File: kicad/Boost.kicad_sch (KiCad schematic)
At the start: 14 parts, among them U15 6.8uH, U16 SX1308

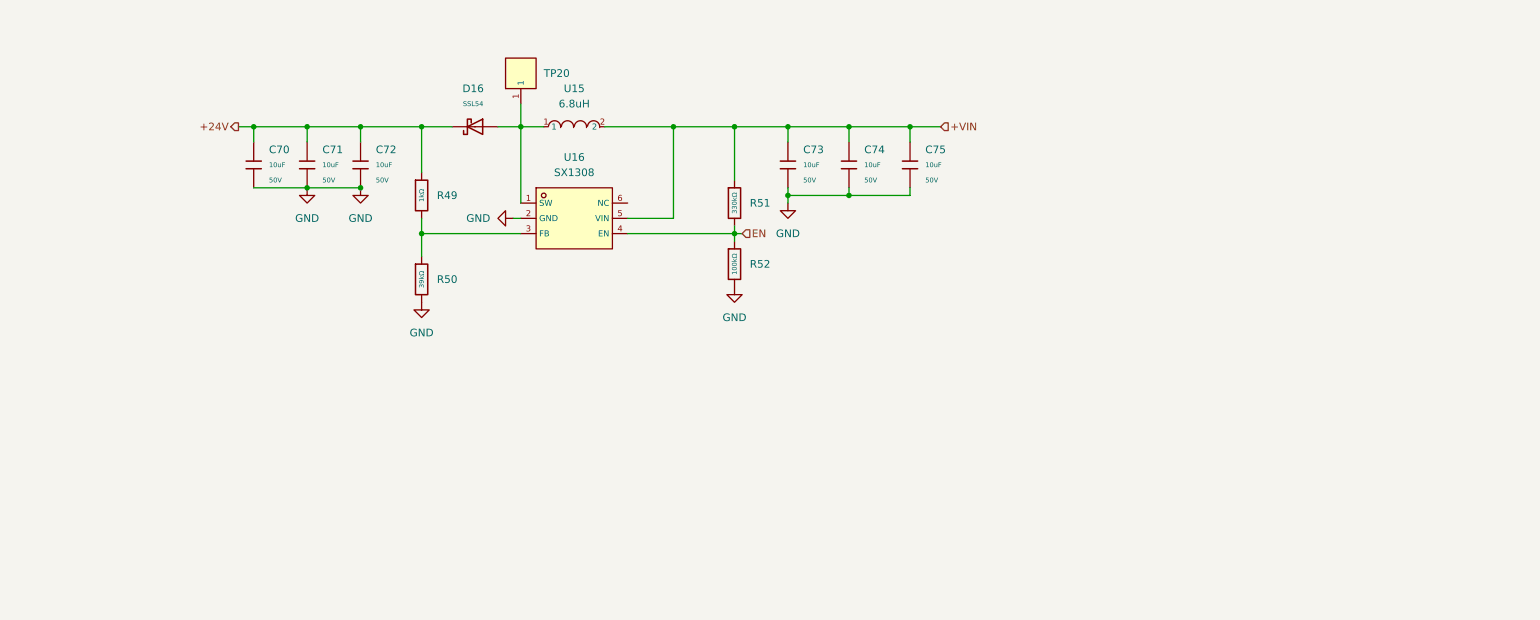
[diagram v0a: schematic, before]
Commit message: Footprint routing completed
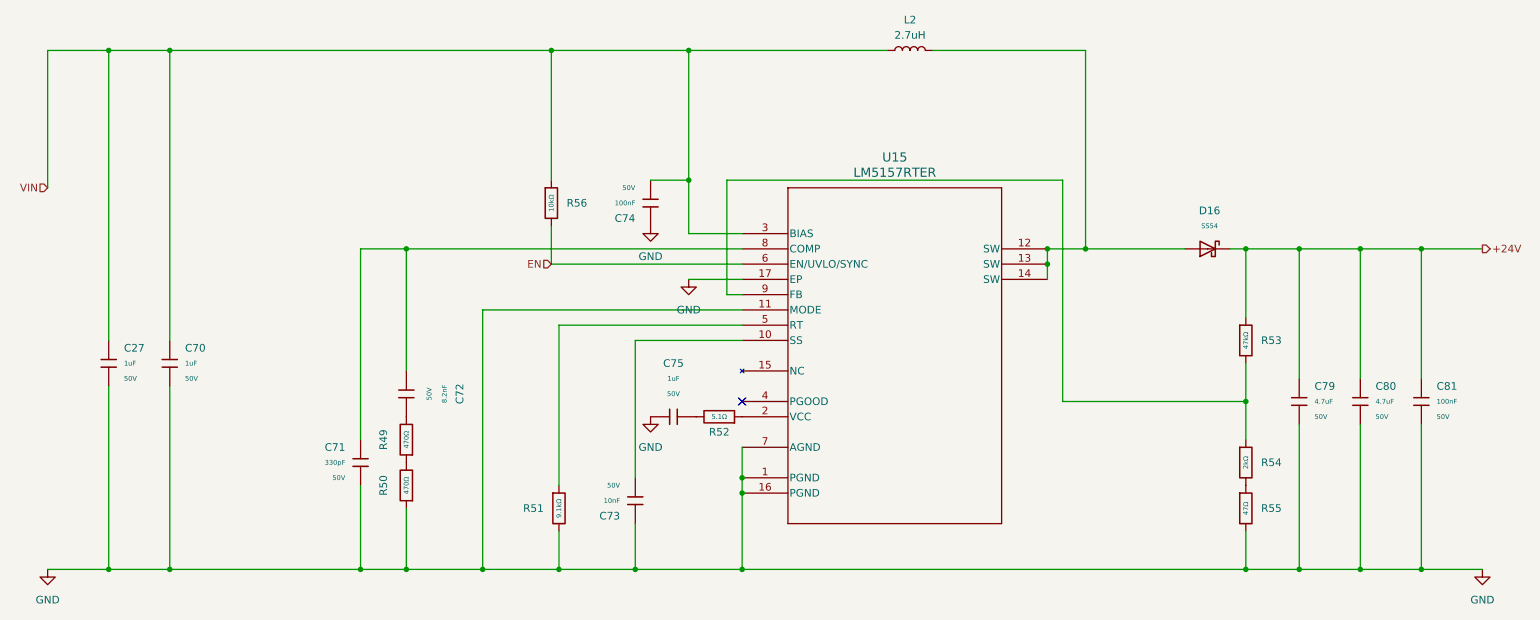
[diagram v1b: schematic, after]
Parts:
- removed C70, C71, C72, C73, C74, C75: 10uF, PCM_JLCPCB:C_0805, symbol 4in-power:0805,10uF,(2)
- removed D16: SSL54, PCM_JLCPCB:D_SMA, symbol 4in-power:Schottky,SSL54
- removed R49: 1kΩ, PCM_JLCPCB:R_0402, symbol 4in-power:0402,1kΩ
- removed R50: 39kΩ, PCM_JLCPCB:R_0402, symbol 4in-power:0402,39kΩ
- removed R51: 330kΩ, PCM_JLCPCB:R_0805, symbol 4in-power:0805,330kΩ
- removed R52: 100kΩ, PCM_JLCPCB:R_0805, symbol 4in-power:0805,100kΩ
- removed TP20: RH-5015, 4in-power:SMD_RH-5015, symbol 4in-power:RH-5015
- removed U15: 6.8uH, 4in-power:IND-SMD_L5.4-W5.2_SLO0530H6R8MTT, symbol 4in-power:SLO0530H6R8MTT
- removed U16: SX1308, 4in-power:SOT-23-6_L2.9-W1.6-P0.95-LS2.8-BL, symbol 4in-power:SX1308
- added C27, C70: 1uF, PCM_JLCPCB:C_0805, symbol PCM_JLCPCB-Capacitors:0805,1uF
- added C71: 330pF, PCM_JLCPCB:C_0603, symbol PCM_JLCPCB-Capacitors:0603,330pF
- added C72: 8.2nF, PCM_JLCPCB:C_0603, symbol PCM_JLCPCB-Capacitors:0603,8.2nF
- added C73: 10nF, PCM_JLCPCB:C_0402, symbol PCM_JLCPCB-Capacitors:0402,10nF
- added C74, C81: 100nF, PCM_JLCPCB:C_0402, symbol PCM_JLCPCB-Capacitors:0402,100nF,(2)
- added C75: 1uF, PCM_JLCPCB:C_0603, symbol PCM_JLCPCB-Capacitors:0603,1uF
- added C79, C80: 4.7uF, PCM_JLCPCB:C_1206, symbol PCM_JLCPCB-Capacitors:1206,4.7uF
- added D16: SS54, PCM_JLCPCB:D_SMA, symbol PCM_JLCPCB-Diodes:Schottky,SS54
- added L2: 2.7uH, 4in-power:IND-SMD_L7.5-W7.5_XAL7030, symbol Device:L
- added R49, R50: 470Ω, PCM_JLCPCB:R_0603, symbol PCM_JLCPCB-Resistors:0603,470Ω
- added R51: 9.1kΩ, PCM_JLCPCB:R_0603, symbol PCM_JLCPCB-Resistors:0603,9.1kΩ
- added R52: 5.1Ω, PCM_JLCPCB:R_0603, symbol PCM_JLCPCB-Resistors:0603,5.1Ω
- added R53: 47kΩ, PCM_JLCPCB:R_0402, symbol PCM_JLCPCB-Resistors:0402,47kΩ
- added R54: 2kΩ, PCM_JLCPCB:R_0402, symbol PCM_JLCPCB-Resistors:0402,2kΩ
- added R55: 47Ω, PCM_JLCPCB:R_0402, symbol PCM_JLCPCB-Resistors:0402,47Ω
- added R56: 10kΩ, PCM_JLCPCB:R_0402, symbol 4in-power:0402,10kΩ
- added U15: LM5157RTER, 4in-power:WQFN-16_L3.0-W3.0-P0.50-TL-EP1.7, symbol Customer:LM5157RTER
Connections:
- net +24V: now also C79.1, C80.1, C81.1, D16.1, R53.1
- net EN: now also R56.2, U15.6 (EN/UVLO/SYNC)
- net GND: now also C27.2, C70.2, C71.1, C73.1, C74.2, C75.2, C79.2, C80.2, C81.2, R50.1, R51.2, R55.2, U15.1 (PGND), U15.11 (MODE), U15.16 (PGND), U15.17 (EP), U15.7 (AGND)
- new net: R51.1, U15.5 (RT)
- new net: C71.2, C72.1, U15.8 (COMP)
- new net: C72.2, R49.2
- new net: R53.2, R54.1, U15.9 (FB)
- new net: R54.2, R55.1
- new net: D16.2, L2.2, U15.12 (SW), U15.13 (SW), U15.14 (SW)
- new net: C75.1, R52.2
- new net: R49.1, R50.2
- new net: C73.2, U15.10 (SS)
- new net: R52.1, U15.2 (VCC)
- new net VIN: C27.1, C70.1, C74.1, L2.1, R56.1, U15.3 (BIAS)
- no-connect marks 0 -> 1
